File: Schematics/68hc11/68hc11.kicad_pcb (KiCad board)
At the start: 2 copper layers, 3 parts, among them U1 MC68HC11A1CC-PLLC, U2 74HC245, U3 74HC373

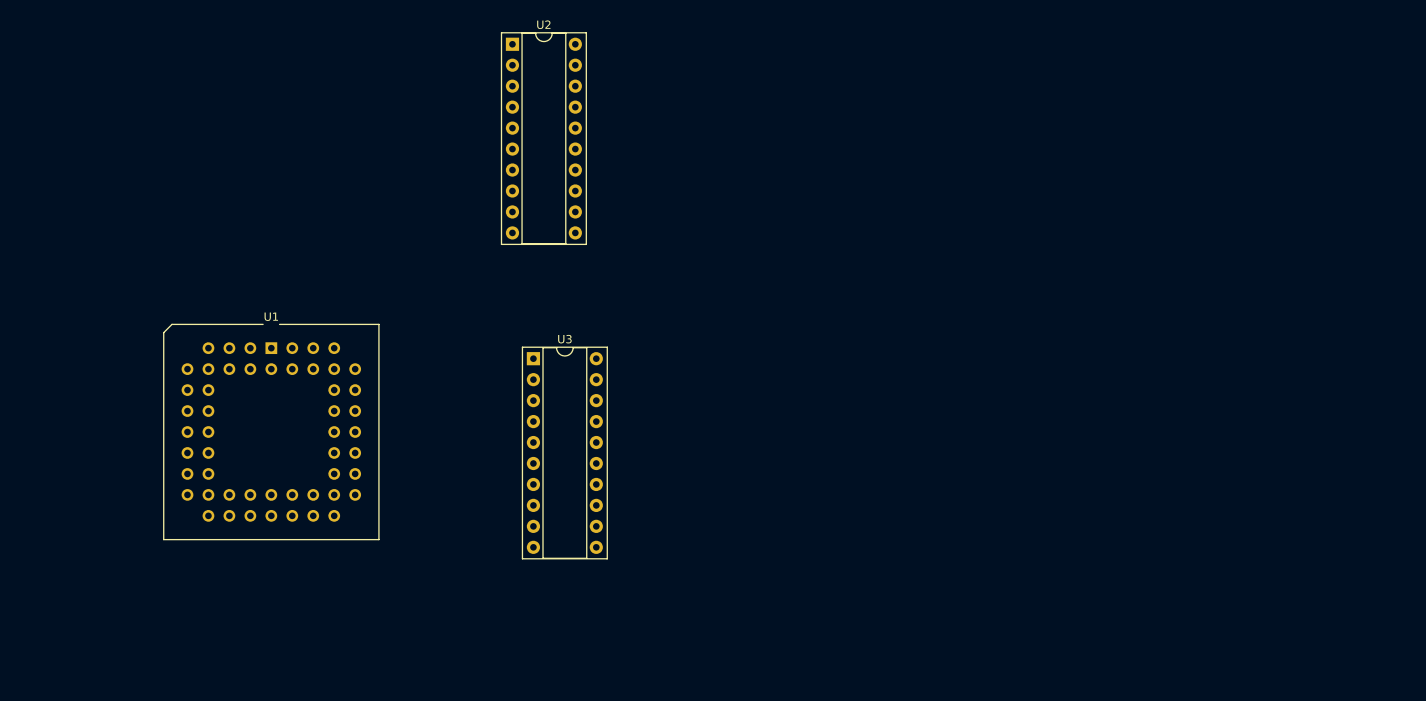
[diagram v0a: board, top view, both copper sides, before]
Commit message: Added some more chips to design
Need to finish Addres block decoding soon.
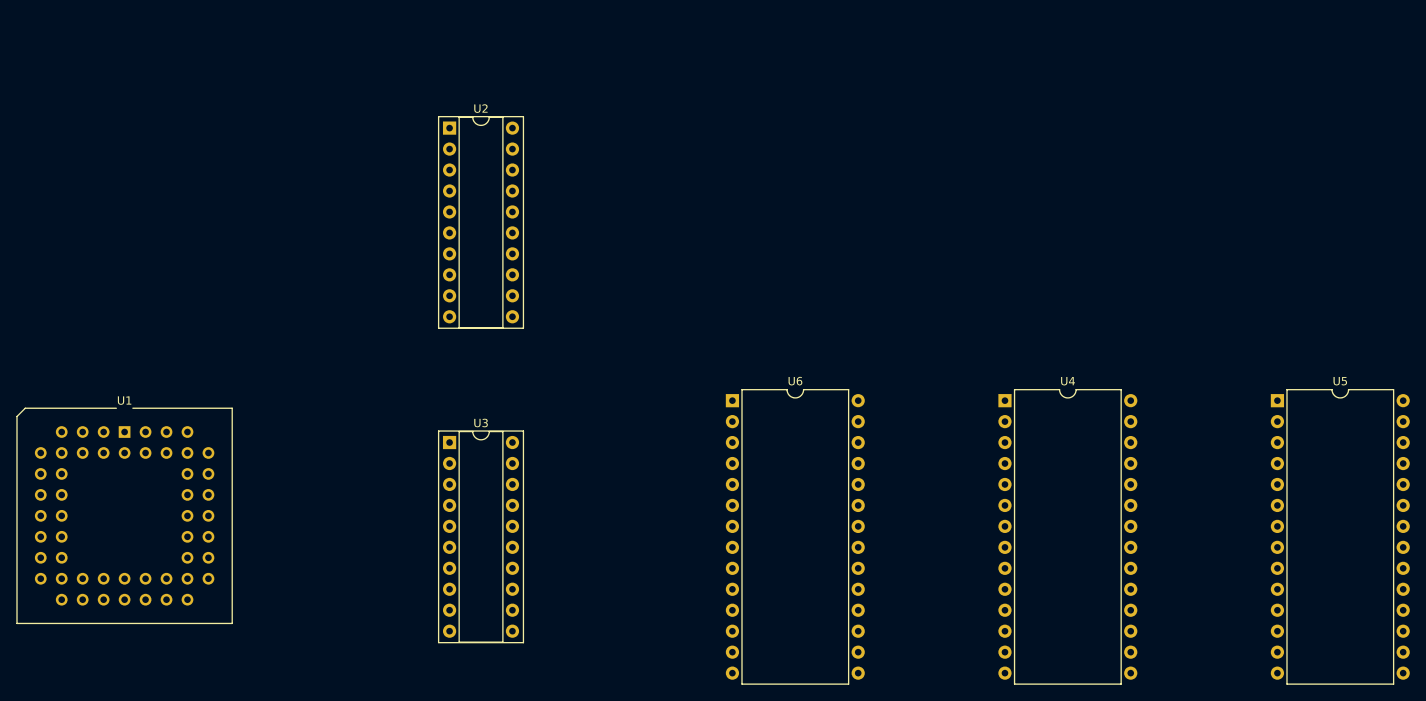
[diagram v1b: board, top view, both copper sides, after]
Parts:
- added U4: 27C64, Package_DIP:DIP-28_W15.24mm, F.Cu at (149.9, 97.8)
- added U5: HM62256BLP, Package_DIP:DIP-28_W15.24mm, F.Cu at (182.9, 97.8)
- added U6: 27C64, Package_DIP:DIP-28_W15.24mm, F.Cu at (116.8, 97.8)
- moved U1 20.5 mm to (43.2, 101.6)
- moved U3 14.4 mm to (82.6, 102.9)
- moved U2 12.7 mm to (82.6, 64.8)
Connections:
- net Net-(U1-Pad4) renamed /AS
- net Net-(U1-Pad6) renamed /R/W

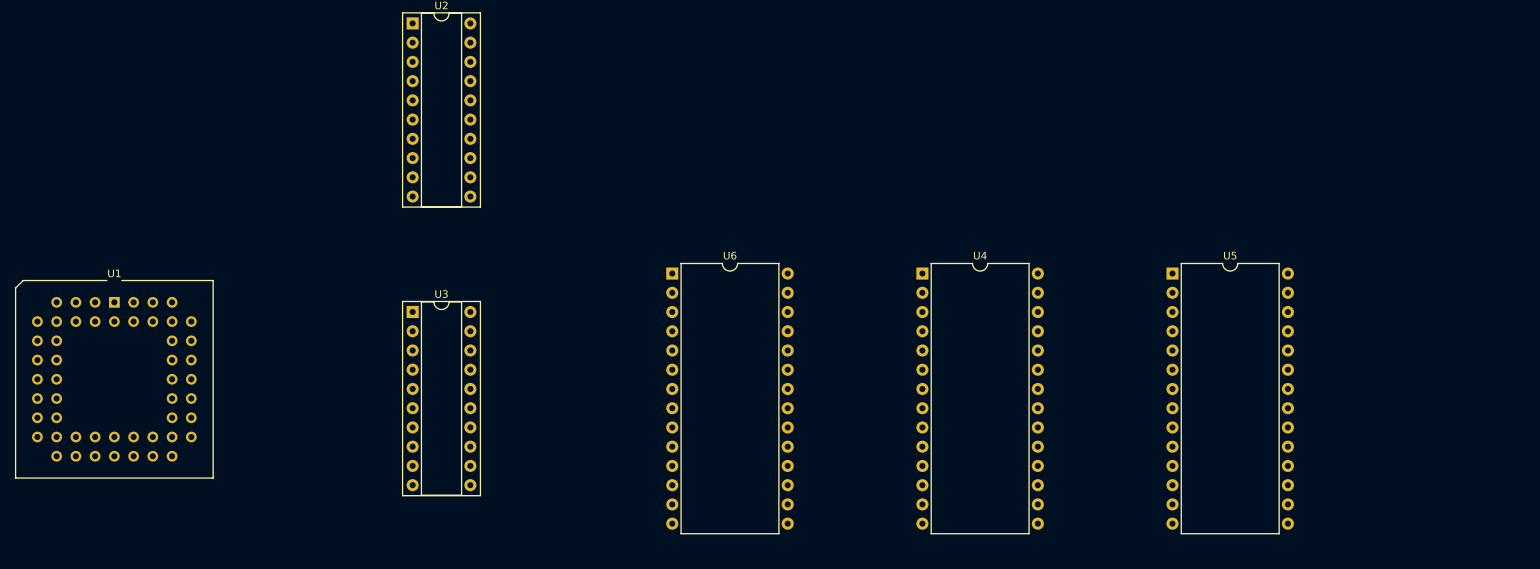
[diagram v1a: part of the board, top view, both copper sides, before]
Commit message: Added more components to schematic
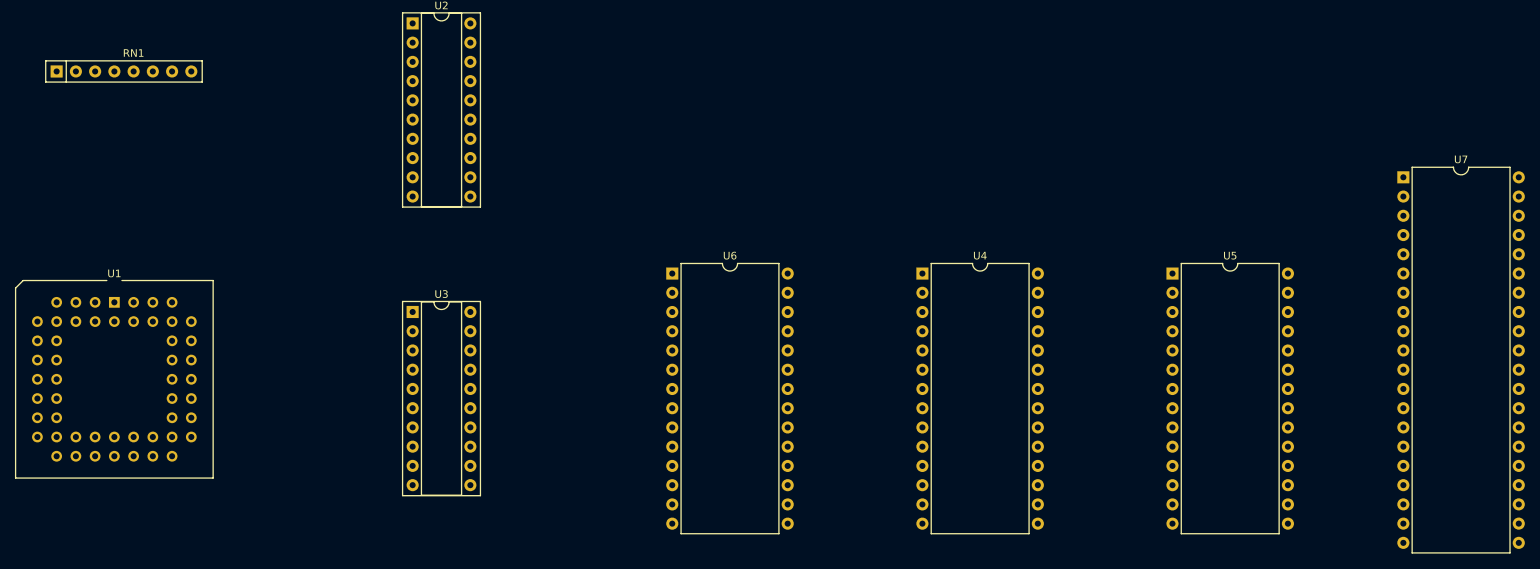
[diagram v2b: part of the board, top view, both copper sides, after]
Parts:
- added RN1: R_Network07_US, Resistor_THT:R_Array_SIP8, F.Cu at (35.6, 71.1)
- added U7: MC68B21, Package_DIP:DIP-40_W15.24mm, F.Cu at (213.4, 85.1)
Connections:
- U1 pad 18: unconnected-(U1-Pad18) -> Net-(U1-Pad18)
- U1 pad 19: unconnected-(U1-Pad19) -> Net-(U1-Pad19)
- U1 pad 2: unconnected-(U1-Pad2) -> Net-(U1-Pad2)
- U1 pad 3: unconnected-(U1-Pad3) -> Net-(U1-Pad3)

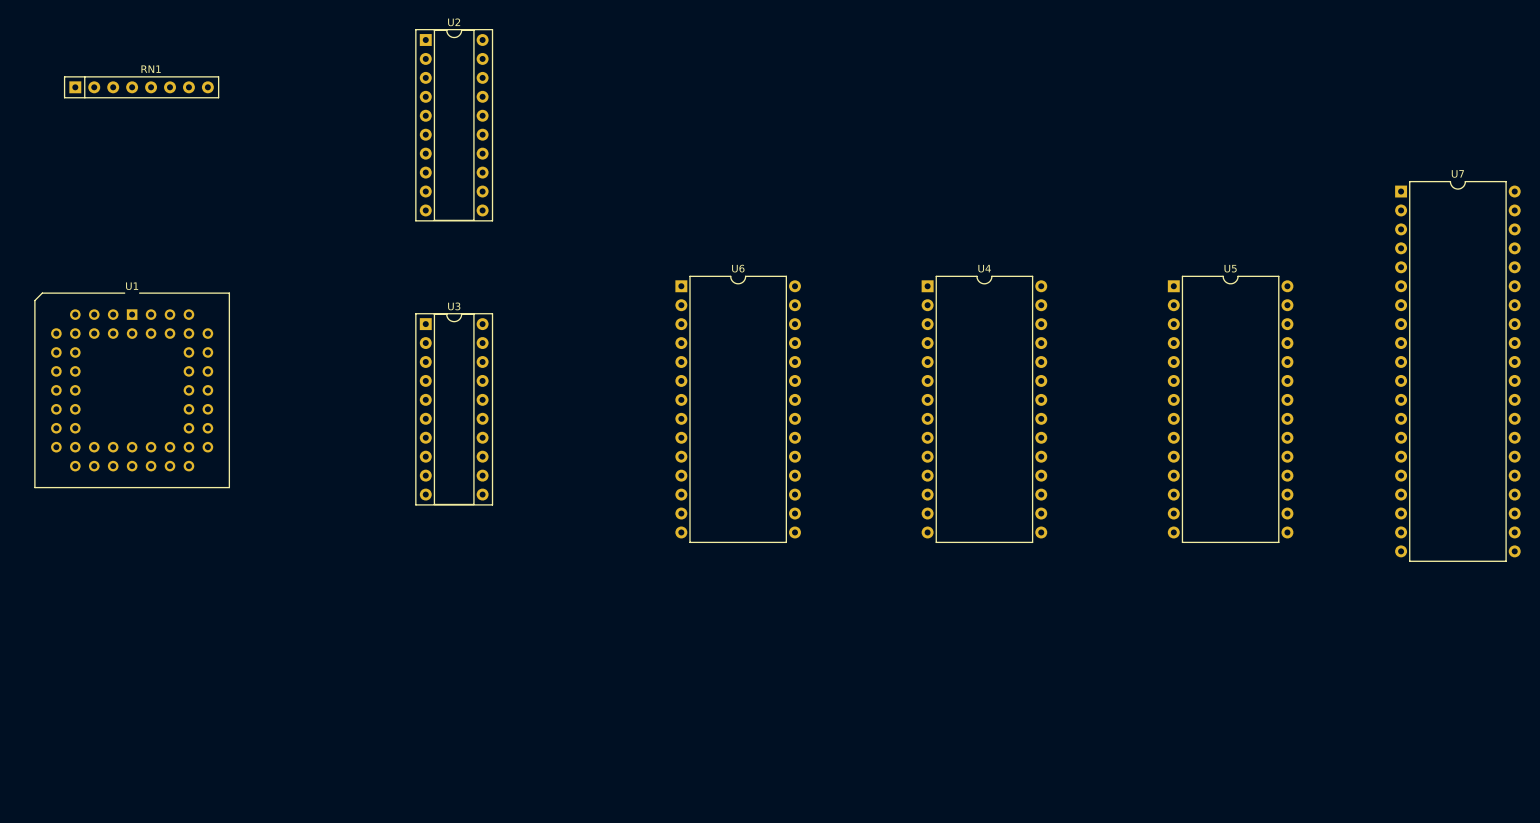
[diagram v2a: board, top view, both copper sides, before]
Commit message: Added MAX232 and DB9 for serial comms
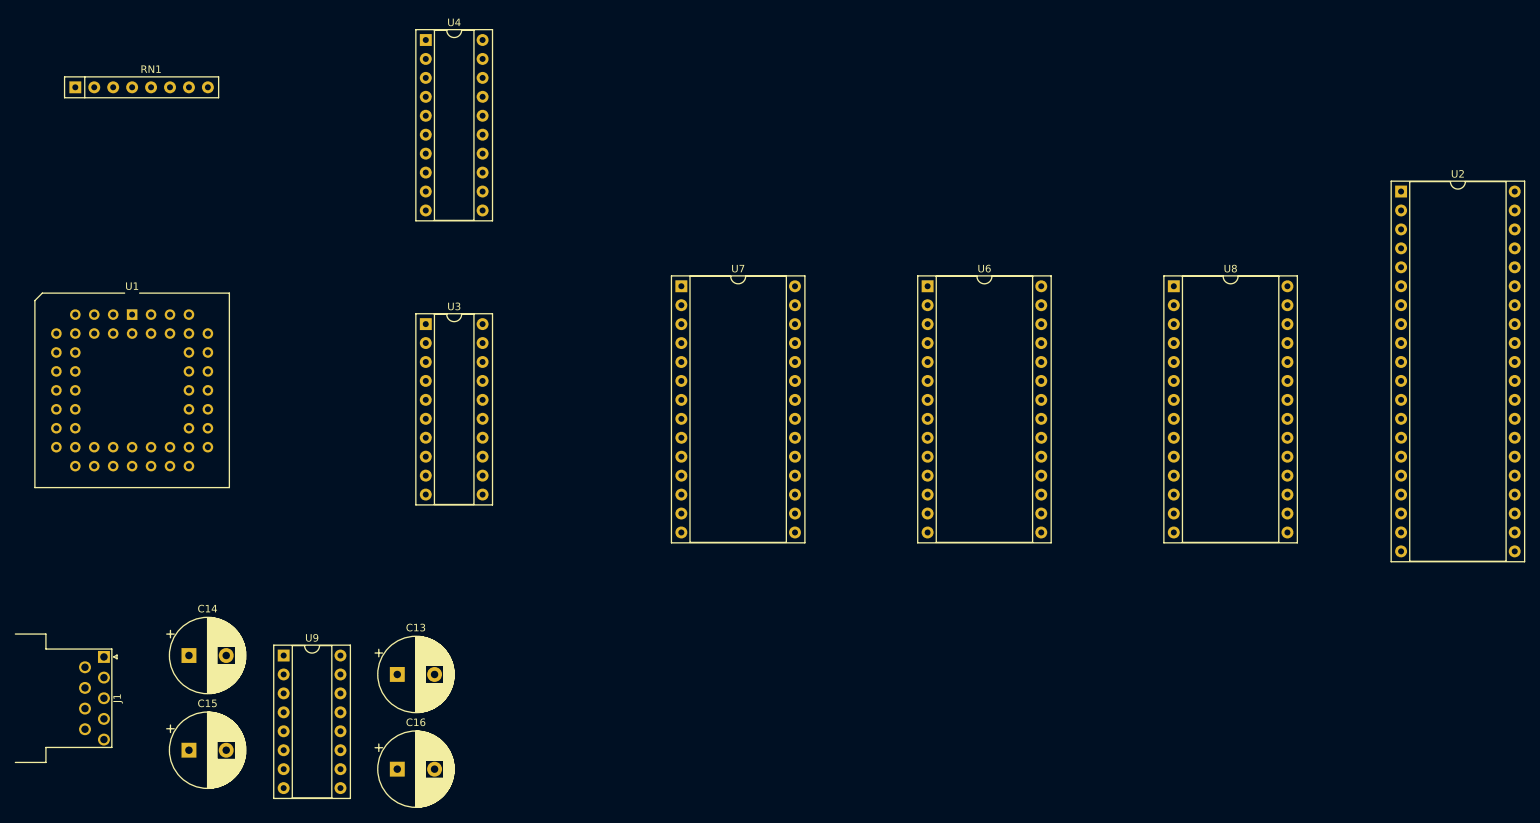
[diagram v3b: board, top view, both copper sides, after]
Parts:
- added C13: 10 uF, Capacitor_THT:CP_Radial_D10.0mm_P5.00mm, F.Cu at (78.7, 149.9)
- added C14: 10 uF, Capacitor_THT:CP_Radial_D10.0mm_P5.00mm, F.Cu at (50.8, 147.3)
- added C15: 19 uF, Capacitor_THT:CP_Radial_D10.0mm_P5.00mm, F.Cu at (50.8, 160.0)
- added C16: 10 uF, Capacitor_THT:CP_Radial_D10.0mm_P5.00mm, F.Cu at (78.7, 162.6)
- added J1: DB9_Female_MountingHoles, Connector_Dsub:DSUB-9_Male_Horizontal_P2.77x2.54mm_EdgePinOffset9.40mm, F.Cu at (39.4, 147.5)
- added U9: MAX232, Package_DIP:DIP-16_W7.62mm_Socket, F.Cu at (63.5, 147.3)
- U2: renamed from U7; footprint Package_DIP:DIP-40_W15.24mm -> Package_DIP:DIP-40_W15.24mm_Socket
- U6: renamed from U4; footprint Package_DIP:DIP-28_W15.24mm -> Package_DIP:DIP-28_W15.24mm_Socket
- U7: renamed from U6; footprint Package_DIP:DIP-28_W15.24mm -> Package_DIP:DIP-28_W15.24mm_Socket
- U8: renamed from U5; footprint Package_DIP:DIP-28_W15.24mm -> Package_DIP:DIP-28_W15.24mm_Socket
- renumbered U2 to U4
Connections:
- net Net-(U1-Pad18) renamed /*XIRQ
- net Net-(U1-Pad19) renamed /*IRQ
- RN1 pad 1: +5V -> VCC
- U1 pad 20: unconnected-(U1-Pad20) -> /RXD
- U1 pad 21: unconnected-(U1-Pad21) -> /TXD
- U1 pad 22: unconnected-(U1-Pad22) -> /MIS
- U1 pad 23: unconnected-(U1-Pad23) -> /MOS
- U1 pad 24: unconnected-(U1-Pad24) -> /SCK
- U1 pad 25: unconnected-(U1-Pad25) -> /SS
- U1 pad 26: +5V -> VCC
- U2 pad 20: +5V -> VCC
- U3 pad 20: +5V -> VCC
- U4 pad 20: +5V -> VCC
- U6 pad 28: +5V -> VCC
- U7 pad 28: +5V -> VCC
- U8 pad 28: +5V -> VCC
